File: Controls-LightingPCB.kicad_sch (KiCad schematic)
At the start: 66 parts, among them J1 MinionConn, J2 12VPWRCONN, SW5 TURN_SIGNAL_SW

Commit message: edits
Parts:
- removed D? (x2): 1N914, Diode_THT:D_DO-35_SOD27_P7.62mm_Horizontal, symbol Diode:1N914
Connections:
- net LEFT_BLINK: now also SW5.1
- net RIGHT_BLINK: now also SW5.4
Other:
- note removed: "The diodes for turn signals are unnecessary"
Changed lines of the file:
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@@
     (stroke (width 0) (type default) (color 0 0 0 0))
   )
-  (wire (pts (xy 197.485 35.56) (xy 186.69 35.56))
+  (wire (pts (xy 171.45 35.56) (xy 197.485 35.56))
     (stroke (width 0) (type default) (color 0 0 0 0))
   )
@@
     (stroke (width 0) (type default) (color 0 0 0 0))
   )
-  (wire (pts (xy 179.07 40.64) (xy 171.45 40.64))
+  (wire (pts (xy 171.45 40.64) (xy 186.69 40.64))
     (stroke (width 0) (type default) (color 0 0 0 0))
   )
@@
   )
   (wire (pts (xy 70.485 145.415) (xy 70.485 143.51))
-    (stroke (width 0) (type default) (color 0 0 0 0))
-  )
-  (wire (pts (xy 171.45 35.56) (xy 179.07 35.56))
     (stroke (width 0) (type default) (color 0 0 0 0))
   )
@@
   )
   (text "12v clk signal\n" (at 137.795 34.29 0)
-    (effects (font (size 1.27 1.27)) (justify left bottom))
-  )
-  (text "The diodes for turn \nsignals are unnecessary" (at 177.165 33.02 0)
     (effects (font (size 1.27 1.27)) (justify left bottom))
   )
@@
     (pin "2")
   )
-  (symbol (lib_id "Diode:1N914") (at 182.88 35.56 180) (unit 1)
-    (in_bom yes) (on_board yes)
-    (property "Reference" "D?" (id 0) (at 182.88 38.1 0))
-    (property "Value" "1N914" (id 1) (at 182.88 40.005 0)
-      (effects (font (size 1.27 1.27)) hide)
-    )
-    (property "Footprint" "Diode_THT:D_DO-35_SOD27_P7.62mm_Horizontal" (id 2) (at 182.88 31.115 0)
-      (effects (font (size 1.27 1.27)) hide)
-    )
-    (property "Datasheet" "http://www.vishay.com/docs/85622/1n914.pdf" (id 3) (at 182.88 35.56 0)
-      (effects (font (size 1.27 1.27)) hide)
-    )
-    (pin "1")
-    (pin "2")
-  )
   (symbol (lib_id "power:GND") (at 52.705 118.745 0) (unit 1)
     (in_bom yes) (on_board yes)
@@
     (pin "2")
   )
-  (symbol (lib_id "Diode:1N914") (at 182.88 40.64 180) (unit 1)
-    (in_bom yes) (on_board yes)
-    (property "Reference" "D?" (id 0) (at 182.88 43.18 0))
-    (property "Value" "1N914" (id 1) (at 182.88 45.085 0)
-      (effects (font (size 1.27 1.27)) hide)
-    )
-    (property "Footprint" "Diode_THT:D_DO-35_SOD27_P7.62mm_Horizontal" (id 2) (at 182.88 36.195 0)
-      (effects (font (size 1.27 1.27)) hide)
-    )
-    (property "Datasheet" "http://www.vishay.com/docs/85622/1n914.pdf" (id 3) (at 182.88 40.64 0)
-      (effects (font (size 1.27 1.27)) hide)
-    )
-    (pin "1")
-    (pin "2")
-  )
   (symbol (lib_id "power:GNDPWR") (at 85.09 31.115 270) (unit 1)
     (in_bom yes) (on_board yes) (fields_autoplaced)
@@
       (reference "D?") (unit 1) (value "PowerOn") (footprint "LED_SMD:LED_0805_2012Metric")
     )
-    (path "/83ce23f9-a191-46c5-a297-c8329075ac3c"
-      (reference "D?") (unit 1) (value "1N914") (footprint "Diode_THT:D_DO-35_SOD27_P7.62mm_Horizontal")
-    )
     (path "/a8089b30-e0c7-4b8c-96d7-0077d76ee2b2"
       (reference "D?") (unit 1) (value "1N914") (footprint "Diode_THT:D_DO-35_SOD27_P7.62mm_Horizontal")
     )
-    (path "/c07c15af-538d-4c74-9cc5-aafa017b511c"
-      (reference "D?") (unit 1) (value "1N914") (footprint "Diode_THT:D_DO-35_SOD27_P7.62mm_Horizontal")
-    )

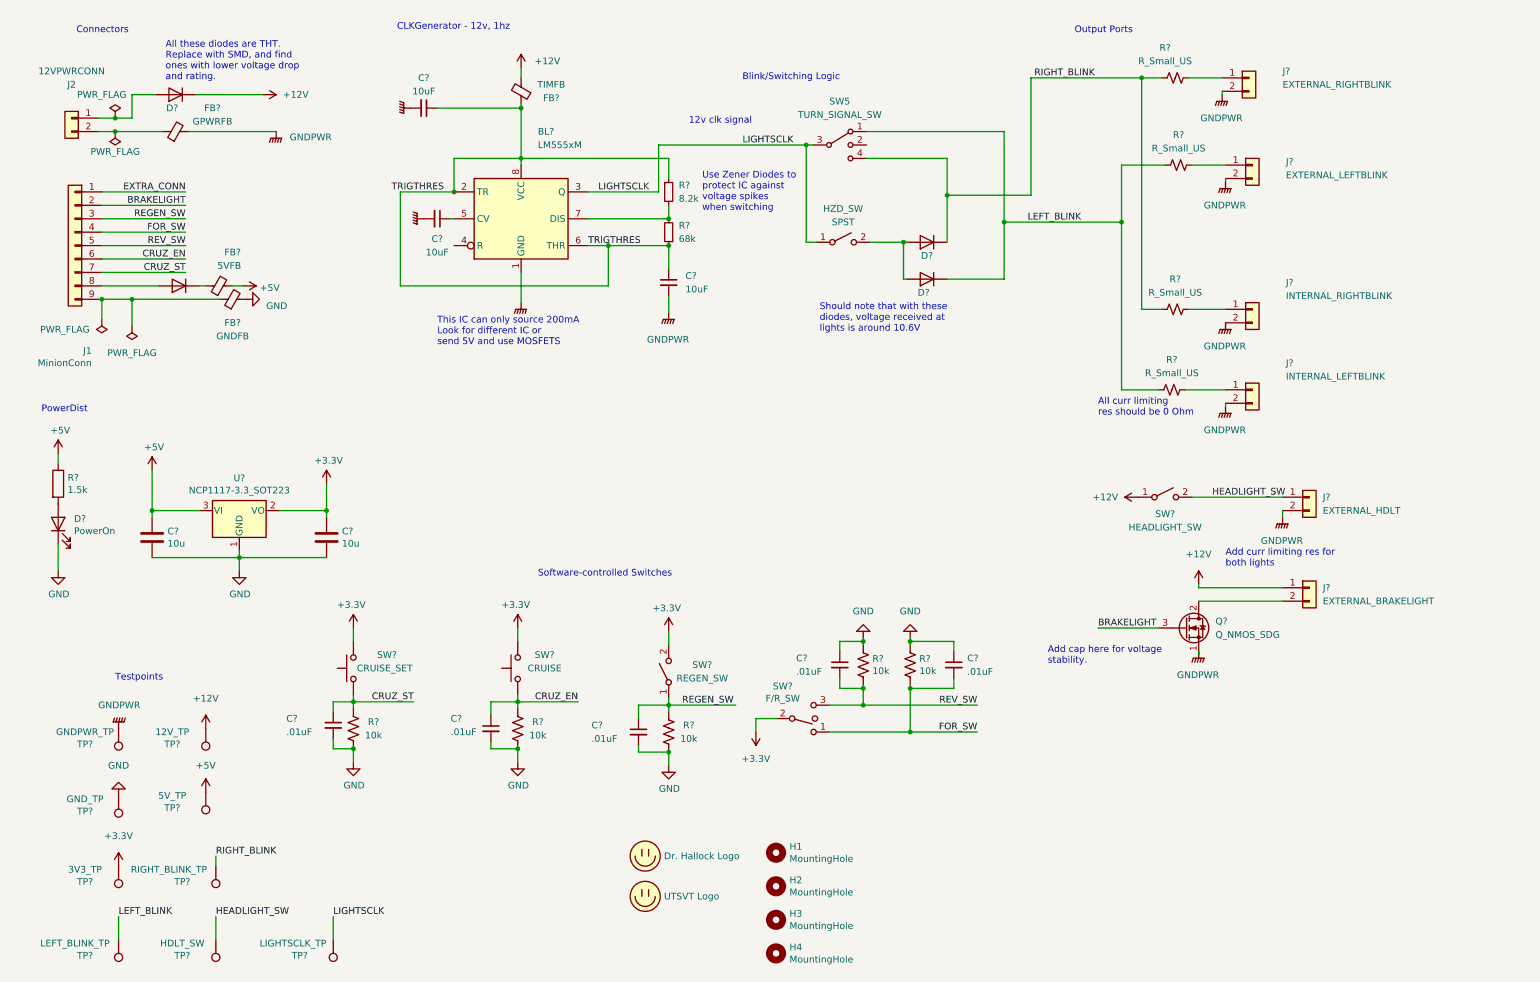
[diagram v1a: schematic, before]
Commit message: Added low side mosfet, small fixes to timer circuit
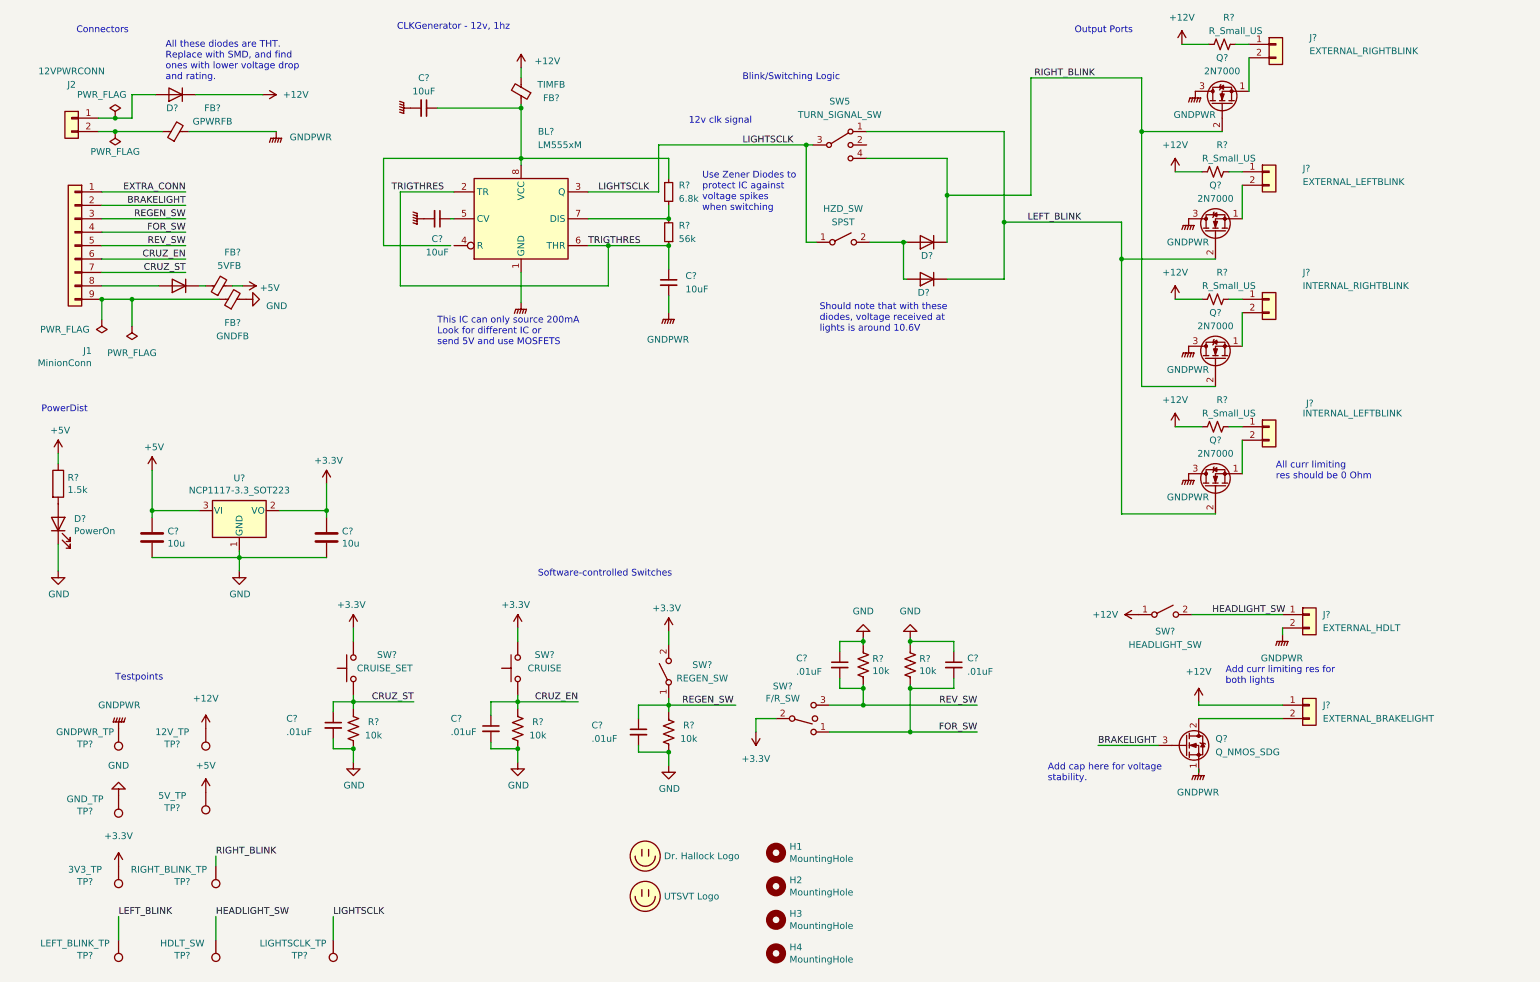
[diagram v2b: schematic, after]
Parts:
- removed R? (x3): R_Small_US, symbol Device:R_Small_US
- added Q? (x4): 2N7000, Package_TO_SOT_THT:TO-92_Inline, symbol Transistor_FET:2N7000
- added R? (x3): R_Small_US, symbol Device:R_Small_US
- R?: value 68k -> 56k
- R?: value 8.2k -> 6.8k
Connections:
- net +12V: now also R?.2, R?.2, R?.2, R?.2
- net GNDPWR: now also Q?.3 (D), Q?.3 (D), Q?.3 (D), Q?.3 (D); no longer J?.2 (Pin_2), J?.2 (Pin_2), J?.2 (Pin_2), J?.2 (Pin_2)
- net LEFT_BLINK: now also Q?.2 (G), Q?.2 (G)
- net RIGHT_BLINK: now also Q?.2 (G), Q?.2 (G); no longer R?.2
- net TRIGTHRES: no longer BL?.8 (VCC), C?.1, FB?.1, R?.1
- net at J?.1 (Pin_1): now also R?.1 (x3)
- new net: J?.2 (Pin_2), Q?.1 (S) (x4)
- new net: BL?.8 (VCC), C?.1, FB?.1, R?.1
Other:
- moved on the sheet: J?, Q?, R?, SW?

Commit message: changed to low-side mosfet switching on IC after switching IC to +5v instead of +12v.
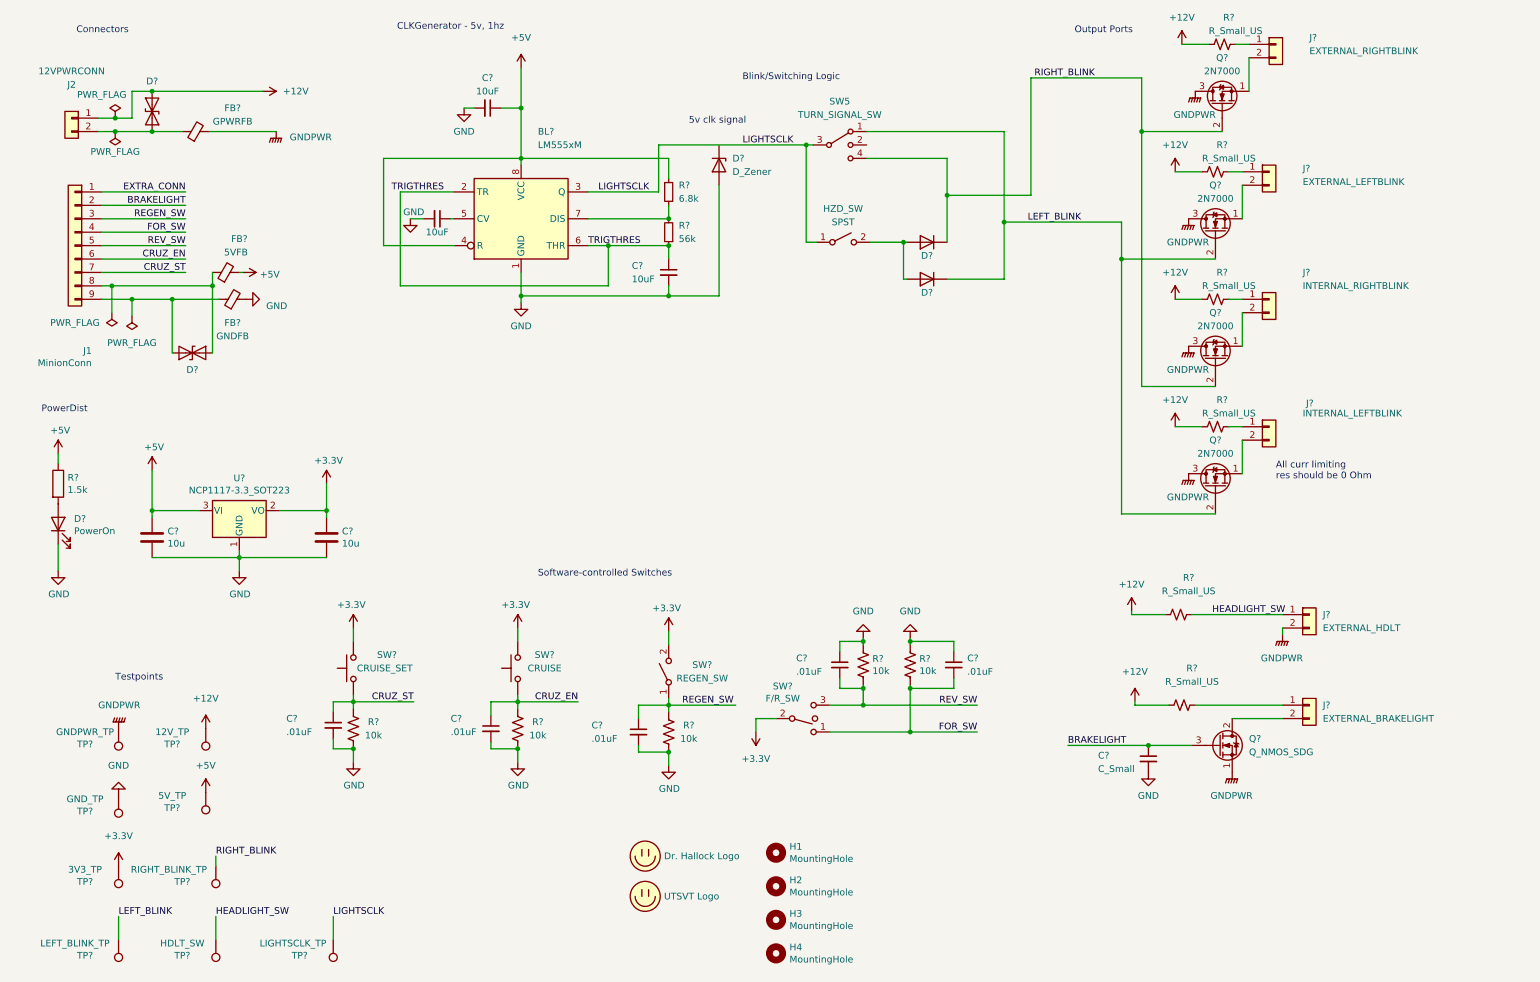
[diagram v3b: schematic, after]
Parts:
- removed D? (x4): 1N914, Diode_THT:D_DO-35_SOD27_P7.62mm_Horizontal, symbol Diode:1N914
- removed FB?: TIMFB, symbol Device:FerriteBead_Small
- removed SW?: HEADLIGHT_SW, symbol Switch:SW_SPST
- added C?: C_Small, symbol Device:C_Small
- added D? (x2): 1N4148WS, Diode_SMD:D_SOD-323, symbol Diode:1N4148WS
- added D? (x2): SD05_SOD323, Diode_SMD:D_SOD-323, symbol Diode:SD05_SOD323
- added D?: D_Zener, symbol Device:D_Zener
- added R? (x2): R_Small_US, symbol Device:R_Small_US
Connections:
- net +12V: now also J2.1 (Pin_1), D?.2 (A2), R?.1, R?.1; no longer J?.1 (Pin_1)
- net +5V: now also BL?.4 (R), BL?.8 (VCC), C?.1, R?.1
- net BRAKELIGHT: now also C?.1
- net GND: now also BL?.1 (GND), C?.2, C?.2, C?.2, C?.2, D?.2 (A)
- net GNDPWR: no longer BL?.1 (GND), C?.2, C?.2, C?.2
- net HEADLIGHT_SW: now also R?.2
- net LEFT_BLINK: now also D?.1 (K)
- net RIGHT_BLINK: now also D?.1 (K)
- net at J1.8 (Pin_8): now also FB?.1, D?.2 (A2)
- net at FB?.1, J1.9 (Pin_9): now also D?.1 (A1)
- net at HZD_SW.2 (B): now also D?.2 (A), D?.2 (A)
- net at FB?.1, J2.2 (Pin_2): now also D?.1 (A1)
- new net: J?.1 (Pin_1), R?.2
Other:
- note added: "5v clk signal"
- note added: "CLKGenerator - 5v, 1hz"
- note removed: "12v clk signal"
- note removed: "Add cap here for voltage stability."
- note removed: "Add curr limiting res for both lights"
- note removed: "All these diodes are THT. Replace with SMD, and find ones with lower voltage drop and rating."
- note removed: "CLKGenerator - 12v, 1hz"
- note removed: "Should note that with these diodes, voltage received at lights is around 10.6V"
- note removed: "This IC can only source 200mA Look for different IC or send 5V and use MOSFETS"
- note removed: "Use Zener Diodes to protect IC against voltage spikes when switching"
- moved on the sheet: C?, FB?, Q?

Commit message: added comments
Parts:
- removed D? (x2): 1N4148WS, Diode_SMD:D_SOD-323, symbol Diode:1N4148WS
- added D? (x2): DIODE, symbol Simulation_SPICE:DIODE
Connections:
- net LEFT_BLINK: now also D?.2 (K)
- net RIGHT_BLINK: now also D?.2 (K)
- net at HZD_SW.2 (B): now also D?.1 (A), D?.1 (A)
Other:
- note added: "Is this a 3.3V signal from Controls board?"
- note added: "These are backwards."
- note added: "These are clamping diodes, not reverse bias protection diodes. Look for TVS one directional"
- note added: "These diodes will have a voltage drop that could prevent a large enough gate voltage. Should keep that in mind"
- moved on the sheet: HZD_SW
